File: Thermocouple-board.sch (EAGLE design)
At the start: 63 parts, among them IC2 LP298XS, J1 RJ45, J11 1X2-3.5MM, J12 1X2-3.5MM, J13 1X2-3.5MM, J14 1X2-3.5MM, J2 RJ45, SW1 PUSHBUTTON, SW2 PUSHBUTTON, U10 MAX31855, U11 MAX31855, U12 MAX31855, U13 MAX31855, U2 EEPROM-I2C, U3 EEPROM-I2C, U5 STM32F030K6

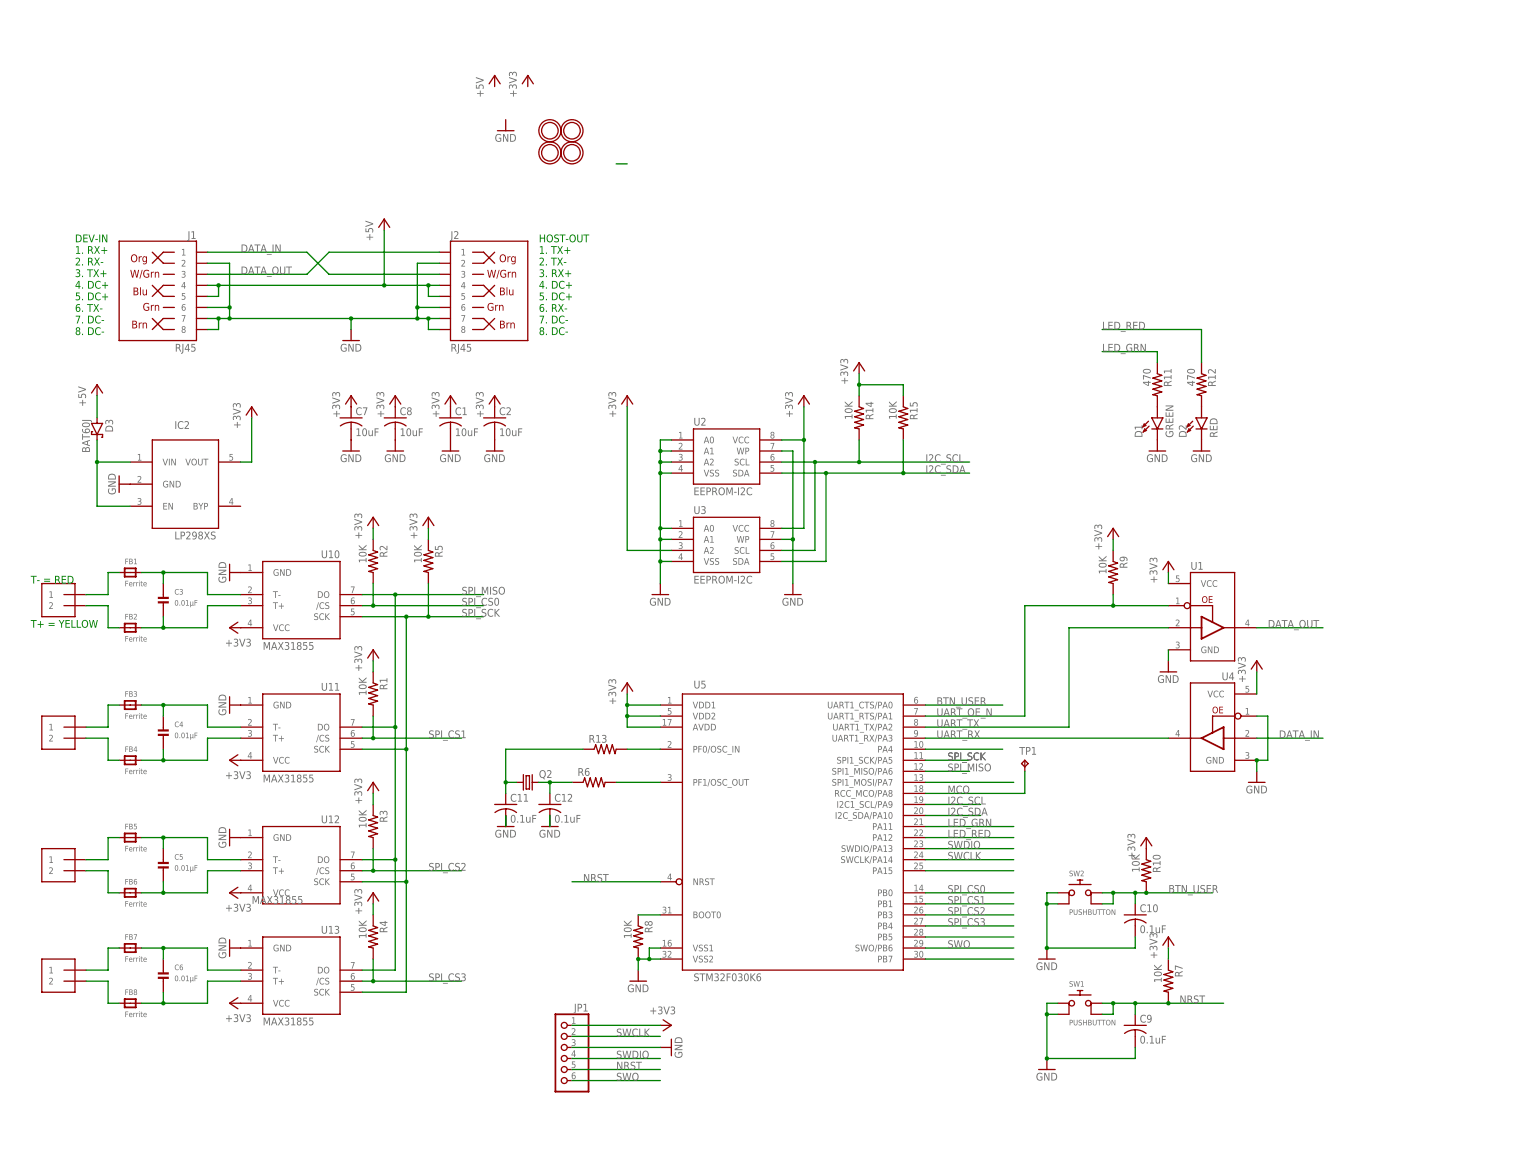
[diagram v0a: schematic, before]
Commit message: WIP Updating with RS-485 transceivers
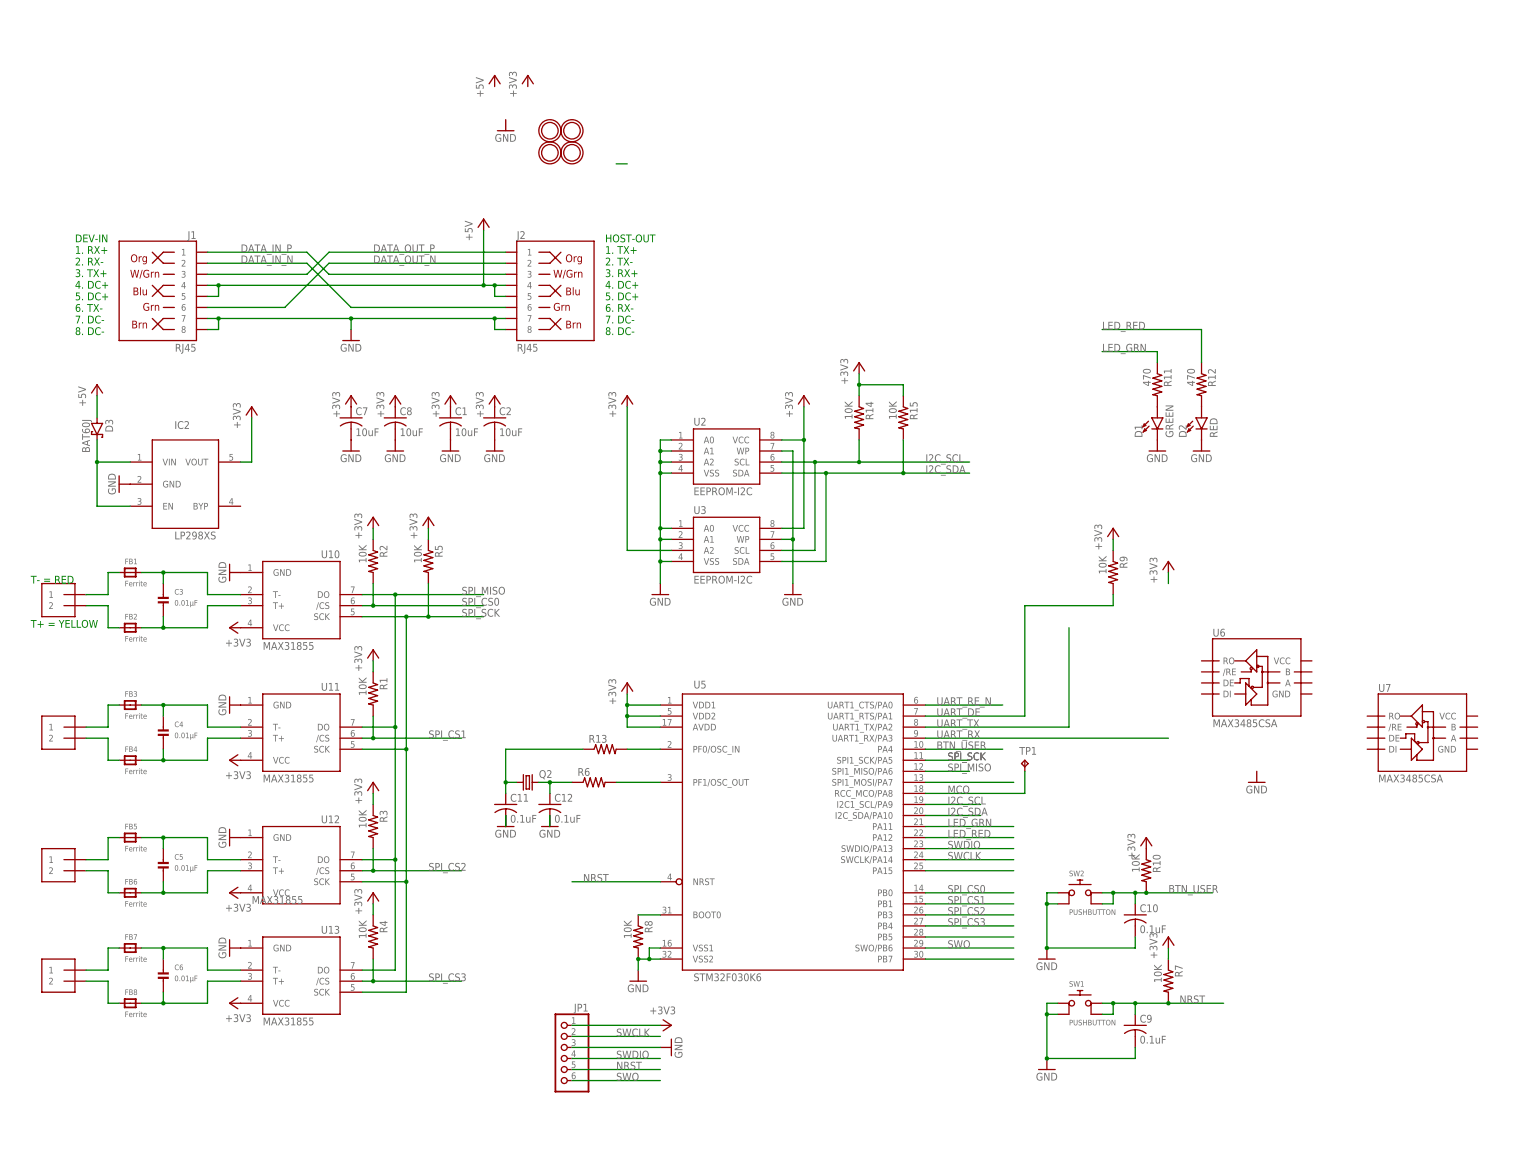
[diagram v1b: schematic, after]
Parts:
- removed U1, U4: (no value), Thermocouple-board:74LVC1G125DBVSOT
- added U6, U7: MAX3485CSA, SparkFun-IC-Comms:RS485SOIC
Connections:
- removed net DATA_IN: J1.1, J2.3, U4.A
- removed net DATA_OUT: J1.3, J2.1, U1.Y
- removed net N$40: U5.PA4
- removed net UART_OE_N: R9.2, U1.!OE, U5.UART1_RTS/PA1
- new net DATA_IN_N: J1.2, J2.6
- new net DATA_IN_P: J1.1, J2.3
- new net DATA_OUT_N: J1.6, J2.2
- new net DATA_OUT_P: J1.3, J2.1
- new net UART_DE: R9.2, U5.UART1_RTS/PA1
- new net UART_RE_N: U5.UART1_CTS/PA0
- net +3V3: no longer U1.VCC, U4.VCC
- net BTN_USER: now also U5.PA4; no longer U5.UART1_CTS/PA0
- net GND: no longer J1.2, J1.6, J2.2, J2.6, U1.GND, U4.!OE, U4.GND
- net UART_RX: no longer U4.Y
- net UART_TX: no longer U1.A
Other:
- moved on the sheet: J2

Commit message: WIP Routing
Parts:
- removed C1, C7: 10uF, adafruit:C-USC0805K
- removed U6, U7: MAX3485CSA, SparkFun-IC-Comms:RS485SOIC
- added C13, C14, C15, C16, C17, C18, C20, C21, C30: 0.1uF, adafruit:C-USC0805K
- added C40: 1uF, adafruit:C-USC0805K
- added C41: 10uF, adafruit:C-USC0805K
- added D4, D5: BAT60J, diode:BAT60J
- added J3: 1981584-1, audio amplifier example:1981584-1
- added R16: 10K, adafruit:R-US_R0805
- added R17: 0, adafruit:R-US_R0805
- added U30: ST3485, SparkFun-IC-Comms:RS485SOIC
- C10, C11, C12, C9: device Thermocouple-board:C-USC0603K -> adafruit:C-USC0805K
- C2: value 10uF -> 0.1uF
- C3, C4, C5, C6: value 0.01µF -> 0.01uF; device microbuilder:CAP_CERAMIC_0805 -> adafruit:C-USC0805K
- JP1: value (none) -> ST-LINK
- Q2: value (none) -> 8MHZ
- R13, R6: value (none) -> 0
- renumbered IC2 to U40, U2 to U20, U3 to U21, U5 to U1
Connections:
- removed net DATA_IN_N: J1.2, J2.6
- removed net DATA_IN_P: J1.1, J2.3
- removed net DATA_OUT_N: J1.6, J2.2
- removed net DATA_OUT_P: J1.3, J2.1
- removed net N$19: D3.C, U40.EN, U40.VIN
- removed net UART_DE: R9.2, U1.UART1_RTS/PA1
- removed net UART_RE_N: U1.UART1_CTS/PA0
- new net DC_P: D3.A, J1.4, J1.5, J2.4, J2.5
- new net N$23: D5.A, JP1.1, R17.1
- new net N$24: D4.A, J3.VBUS
- new net PORT0_N: J1.2, J2.2, U30.B
- new net PORT0_P: J1.1, J2.1, U30.A
- new net PORT1_N: J1.6, J2.6
- new net PORT1_P: J1.3, J2.3
- new net UART_CTS: U1.UART1_CTS/PA0, U30./RE
- new net UART_RTS: R9.1, U1.UART1_RTS/PA1, U30.DE
- net +3V3: now also C13.1, C14.1, C15.1, C16.1, C17.1, C18.1, C20.1, C21.1, C30.1, C41.1, R16.1, R17.2, U30.VCC; no longer C1.1, C7.1, JP1.1, R9.1
- net +5V: now also C40.1, D3.C, D4.C, D5.C, U40.EN, U40.VIN; no longer D3.A, J1.4, J1.5, J2.4, J2.5
- net BTN_USER: now also C9.1; no longer C10.1
- net GND: now also C13.2, C14.2, C15.2, C16.2, C17.2, C18.2, C20.2, C21.2, C30.2, C40.2, C41.2, J3.GND, J3.S1, R9.2, U30.GND; no longer C1.2, C7.2
- net N$10: now also C4.2; no longer C4.P$2
- net N$12: now also C5.1; no longer C5.P$1
- net N$14: now also C5.2; no longer C5.P$2
- net N$16: now also C6.1; no longer C6.P$1
- net N$18: now also C6.2; no longer C6.P$2
- net N$2: now also C11.1; no longer C12.1
- net N$3: now also C12.1; no longer C11.1
- net N$4: now also C3.1; no longer C3.P$1
- net N$6: now also C3.2; no longer C3.P$2
- net N$8: now also C4.1; no longer C4.P$1
- net NRST: now also C10.1; no longer C9.1
- net UART_RX: now also R16.2, U30.RO
- net UART_TX: now also U30.DI
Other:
- note added: "ETHERNET"
- note added: "PWR ONLY"
- moved on the sheet: C2, D3, JP1, R6, R9, TP1

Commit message: WIP Routing
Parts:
- added U$3: MOUNTINGHOLE2.0, microbuilder:MOUNTINGHOLE2.0
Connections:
- net N$21 renamed BOOT0
- net SPI_CS0: now also R1.2; no longer R2.2
- net SPI_CS1: now also R2.2; no longer R1.2
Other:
- moved on the sheet: R1, R2, R8
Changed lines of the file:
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@@
 <part name="+3V6" library="supply1" deviceset="+3V3" device=""/>
 <part name="GND7" library="supply1" deviceset="GND" device=""/>
+<part name="R2" library="adafruit" deviceset="R-US_" device="R0805" value="10K"/>
 <part name="R1" library="adafruit" deviceset="R-US_" device="R0805" value="10K"/>
-<part name="R2" library="adafruit" deviceset="R-US_" device="R0805" value="10K"/>
 <part name="+3V8" library="supply1" deviceset="+3V3" device=""/>
 <part name="FB1" library="microbuilder" deviceset="FERRITE" device="_0805" value="Ferrite"/>
@@
 <part name="+3V31" library="supply1" deviceset="+3V3" device=""/>
 <part name="GND33" library="supply1" deviceset="GND" device=""/>
+<part name="U$3" library="microbuilder" deviceset="MOUNTINGHOLE" device="2.0"/>
 </parts>
 <sheets>
@@
 <attribute name="VALUE" x="-25.4" y="25.4" size="1.778" layer="96"/>
 </instance>
-<instance part="R1" gate="G$1" x="35.56" y="-7.62" smashed="yes" rot="R270">
+<instance part="R2" gate="G$1" x="35.56" y="-7.62" smashed="yes" rot="R270">
 <attribute name="NAME" x="37.0586" y="-3.81" size="1.778" layer="95" rot="R270"/>
 <attribute name="VALUE" x="32.258" y="-3.81" size="1.778" layer="96" rot="R270"/>
 </instance>
-<instance part="R2" gate="G$1" x="35.56" y="22.86" smashed="yes" rot="R270">
+<instance part="R1" gate="G$1" x="35.56" y="22.86" smashed="yes" rot="R270">
 <attribute name="NAME" x="37.0586" y="26.67" size="1.778" layer="95" rot="R270"/>
 <attribute name="VALUE" x="32.258" y="26.67" size="1.778" layer="96" rot="R270"/>
@@
 <attribute name="VALUE" x="91.44" y="-10.16" size="1.778" layer="96" rot="R90"/>
 </instance>
-<instance part="GND11" gate="1" x="96.52" y="-73.66" smashed="yes">
-<attribute name="VALUE" x="93.98" y="-76.2" size="1.778" layer="96"/>
+<instance part="GND11" gate="1" x="88.9" y="-73.66" smashed="yes">
+<attribute name="VALUE" x="86.36" y="-76.2" size="1.778" layer="96"/>
 </instance>
 <instance part="Q2" gate="G$1" x="71.12" y="-27.94" smashed="yes">
@@
 <attribute name="VALUE" x="215.9" y="-68.58" size="1.778" layer="96" rot="R90"/>
 </instance>
-<instance part="R8" gate="G$1" x="96.52" y="-63.5" smashed="yes" rot="R270">
-<attribute name="NAME" x="98.0186" y="-59.69" size="1.778" layer="95" rot="R270"/>
-<attribute name="VALUE" x="93.218" y="-59.69" size="1.778" layer="96" rot="R270"/>
+<instance part="R8" gate="G$1" x="88.9" y="-63.5" smashed="yes" rot="R270">
+<attribute name="NAME" x="90.3986" y="-59.69" size="1.778" layer="95" rot="R270"/>
+<attribute name="VALUE" x="85.598" y="-59.69" size="1.778" layer="96" rot="R270"/>
 </instance>
 <instance part="GND16" gate="1" x="101.6" y="15.24" smashed="yes">
@@
 <attribute name="VALUE" x="241.3" y="2.54" size="1.778" layer="96"/>
 </instance>
+<instance part="U$3" gate="G$1" x="71.12" y="121.92" smashed="yes"/>
 </instances>
 <busses>
@@
 <wire x1="101.6" y1="-68.58" x2="99.06" y2="-68.58" width="0.1524" layer="91"/>
 <pinref part="GND11" gate="1" pin="GND"/>
-<wire x1="96.52" y1="-68.58" x2="96.52" y2="-71.12" width="0.1524" layer="91"/>
+<wire x1="88.9" y1="-68.58" x2="88.9" y2="-71.12" width="0.1524" layer="91"/>
 <wire x1="101.6" y1="-66.04" x2="99.06" y2="-66.04" width="0.1524" layer="91"/>
 <wire x1="99.06" y1="-66.04" x2="99.06" y2="-68.58" width="0.1524" layer="91"/>
-<wire x1="99.06" y1="-68.58" x2="96.52" y2="-68.58" width="0.1524" layer="91"/>
-<junction x="96.52" y="-68.58"/>
+<wire x1="99.06" y1="-68.58" x2="88.9" y2="-68.58" width="0.1524" layer="91"/>
+<junction x="88.9" y="-68.58"/>
 <pinref part="R8" gate="G$1" pin="2"/>
 <junction x="99.06" y="-68.58"/>
@@
 <segment>
 <pinref part="U10" gate="G$1" pin="/CS"/>
-<pinref part="R2" gate="G$1" pin="2"/>
+<pinref part="R1" gate="G$1" pin="2"/>
 <label x="55.88" y="12.7" size="1.778" layer="95"/>
 <wire x1="33.02" y1="12.7" x2="35.56" y2="12.7" width="0.1524" layer="91"/>
@@
 <segment>
 <pinref part="+3V8" gate="G$1" pin="+3V3"/>
-<pinref part="R2" gate="G$1" pin="1"/>
+<pinref part="R1" gate="G$1" pin="1"/>
 <wire x1="35.56" y1="30.48" x2="35.56" y2="27.94" width="0.1524" layer="91"/>
 </segment>
@@
 <segment>
 <pinref part="+3V2" gate="G$1" pin="+3V3"/>
-<pinref part="R1" gate="G$1" pin="1"/>
+<pinref part="R2" gate="G$1" pin="1"/>
 <wire x1="35.56" y1="0" x2="35.56" y2="-2.54" width="0.1524" layer="91"/>
 </segment>
@@
 <wire x1="35.56" y1="-17.78" x2="55.88" y2="-17.78" width="0.1524" layer="91"/>
 <label x="48.26" y="-17.78" size="1.778" layer="95"/>
-<pinref part="R1" gate="G$1" pin="2"/>
+<pinref part="R2" gate="G$1" pin="2"/>
 <wire x1="35.56" y1="-12.7" x2="35.56" y2="-17.78" width="0.1524" layer="91"/>
 <junction x="35.56" y="-17.78"/>
@@
 </segment>
 </net>
-<net name="N$21" class="0">
+<net name="BOOT0" class="0">
 <segment>
 <pinref part="R8" gate="G$1" pin="1"/>
-<wire x1="101.6" y1="-58.42" x2="96.52" y2="-58.42" width="0.1524" layer="91"/>
+<wire x1="101.6" y1="-58.42" x2="88.9" y2="-58.42" width="0.1524" layer="91"/>
 <pinref part="U1" gate="G$1" pin="BOOT0"/>
-</segment>
-</net>
+<label x="91.44" y="-58.42" size="1.778" layer="95"/>
+</segment>
+</net>

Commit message: WIP routing
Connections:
- removed net N$20: R6.2, U1.PF1/OSC_OUT
- removed net N$22: R13.2, U1.PF0/OSC_IN
- net SPI_MISO: now also R5.2
- net SPI_SCK: no longer R5.2
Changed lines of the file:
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@@
-</segment>
-</net>
-<net name="N$20" class="0">
-<segment>
-<wire x1="101.6" y1="-27.94" x2="93.98" y2="-27.94" width="0.1524" layer="91"/>
-<pinref part="R6" gate="G$1" pin="2"/>
-<pinref part="U1" gate="G$1" pin="PF1/OSC_OUT"/>
 </segment>
 </net>
@@
 <wire x1="43.18" y1="-76.2" x2="33.02" y2="-76.2" width="0.1524" layer="91"/>
 <junction x="43.18" y="-50.8"/>
-<wire x1="43.18" y1="10.16" x2="48.26" y2="10.16" width="0.1524" layer="91"/>
 <label x="55.88" y="10.16" size="1.778" layer="95"/>
-<pinref part="R5" gate="G$1" pin="2"/>
-<wire x1="48.26" y1="17.78" x2="48.26" y2="10.16" width="0.1524" layer="91"/>
-<junction x="48.26" y="10.16"/>
-<wire x1="48.26" y1="10.16" x2="60.96" y2="10.16" width="0.1524" layer="91"/>
+<wire x1="43.18" y1="10.16" x2="60.96" y2="10.16" width="0.1524" layer="91"/>
 </segment>
 </net>
@@
 <wire x1="40.64" y1="-71.12" x2="33.02" y2="-71.12" width="0.1524" layer="91"/>
 <junction x="40.64" y="-45.72"/>
-<wire x1="40.64" y1="15.24" x2="60.96" y2="15.24" width="0.1524" layer="91"/>
+<wire x1="40.64" y1="15.24" x2="48.26" y2="15.24" width="0.1524" layer="91"/>
 <junction x="40.64" y="15.24"/>
 <label x="55.88" y="15.24" size="1.778" layer="95"/>
+<pinref part="R5" gate="G$1" pin="2"/>
+<wire x1="48.26" y1="15.24" x2="60.96" y2="15.24" width="0.1524" layer="91"/>
+<wire x1="48.26" y1="17.78" x2="48.26" y2="15.24" width="0.1524" layer="91"/>
+<junction x="48.26" y="15.24"/>
 </segment>
 </net>
@@
 </segment>
 </net>
-<net name="N$22" class="0">
-<segment>
-<pinref part="U1" gate="G$1" pin="PF0/OSC_IN"/>
-<wire x1="93.98" y1="-20.32" x2="101.6" y2="-20.32" width="0.1524" layer="91"/>
-<pinref part="R13" gate="G$1" pin="2"/>
-</segment>
-</net>

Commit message: WIP routing
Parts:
- removed C11, C12, C18: 0.1uF, adafruit:C-USC0805K
- removed C8: 10uF, adafruit:C-USC0805K
- removed Q2: 8MHZ, adafruit:CRYSTALHC49U-V
- removed R13, R6: 0, adafruit:R-US_R0603
- removed U$3: MOUNTINGHOLE2.0, microbuilder:MOUNTINGHOLE2.0
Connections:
- net DC_P renamed POE_PWR
- net PORT0_N renamed DN_LINK_B
- net PORT0_P renamed DN_LINK_A
- net PORT1_N renamed UP_LINK_B
- net PORT1_P renamed UP_LINK_A
- removed net N$2: C11.1, Q2.2, R6.1
- removed net N$3: C12.1, Q2.1, R13.1
- net +3V3: no longer C18.1, C8.1
- net GND: no longer C11.2, C12.2, C18.2, C8.2
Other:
- moved on the sheet: TP1
